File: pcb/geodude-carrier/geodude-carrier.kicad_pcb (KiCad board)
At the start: 2 copper layers, 112.5 x 135.2 mm, 43 parts, among them J1 12V, J2 12V, J3 GND, J31 SCL, J32 SDA, J34 3V3, J37 5V, J39 GND_L, J4 GND, J40 SCL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

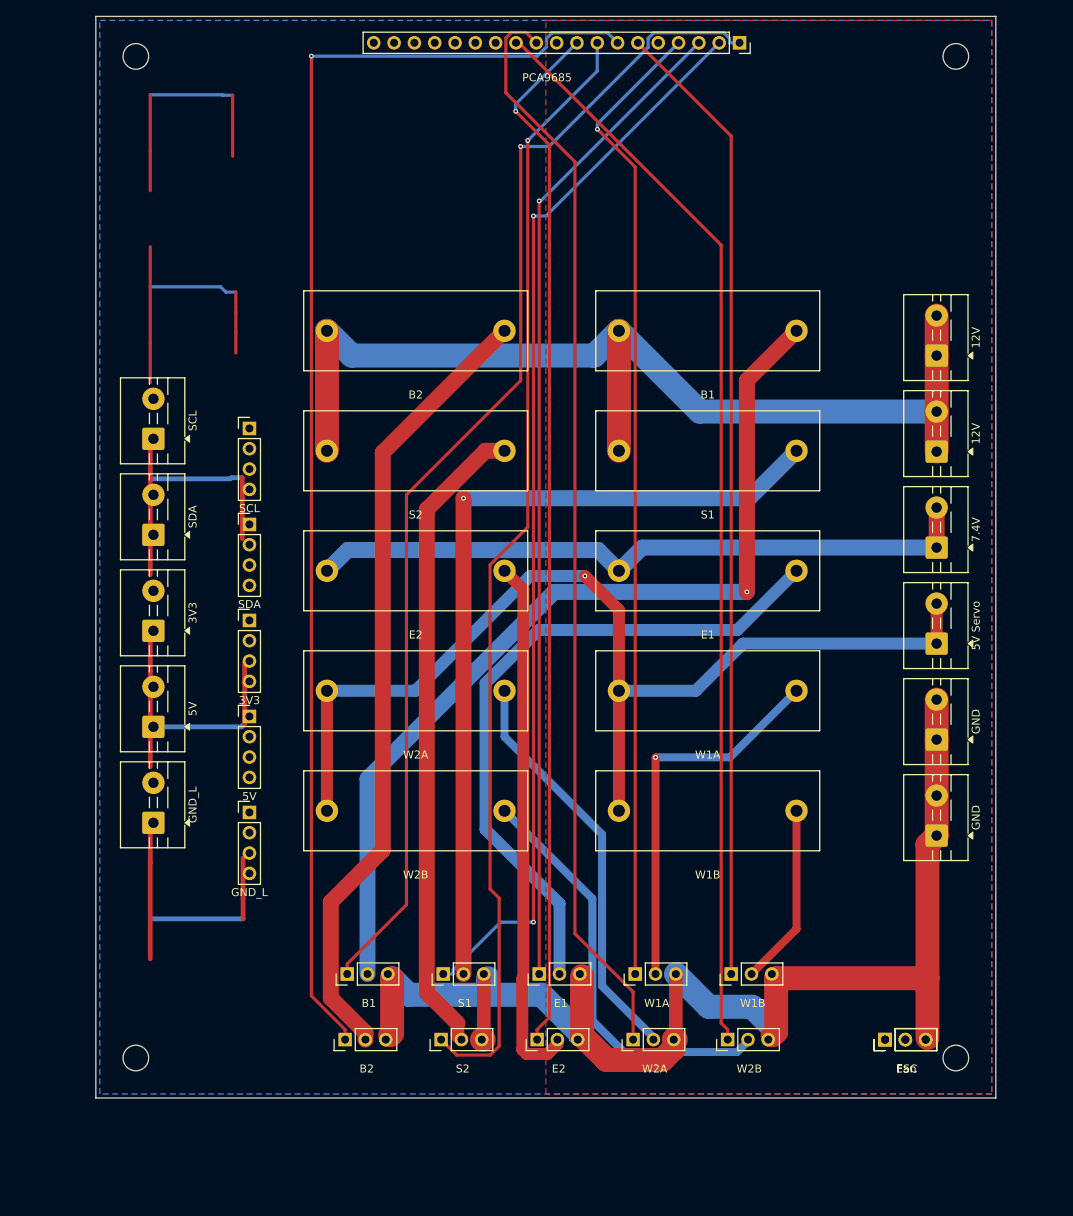
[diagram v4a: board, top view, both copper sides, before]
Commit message: Mounting holes 50mm horizontal spacing, centred
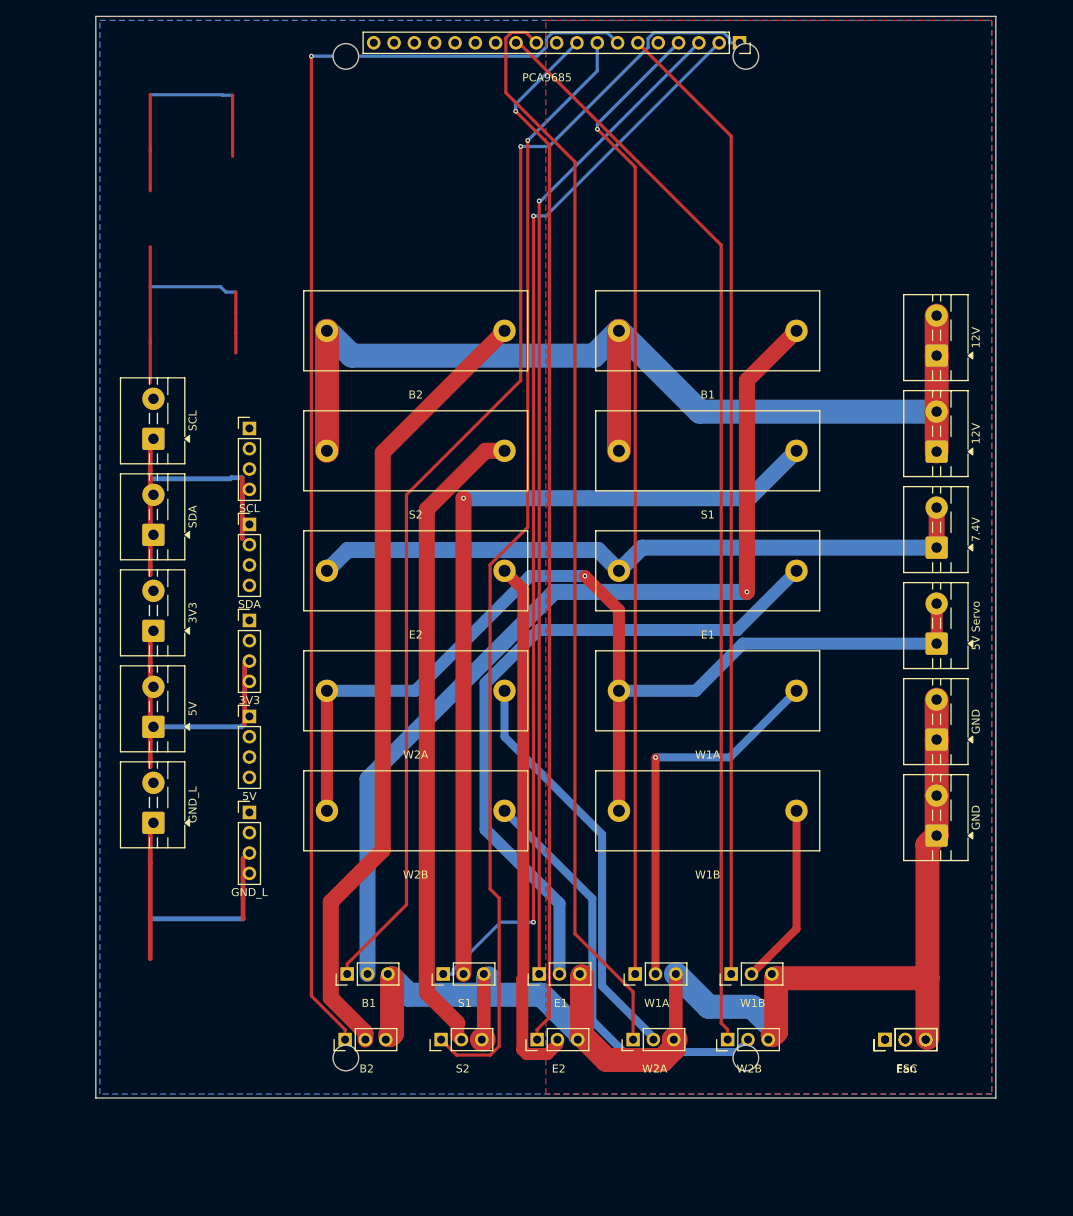
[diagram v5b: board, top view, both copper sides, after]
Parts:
- moved MH2 26.2 mm to (99.0, 9.60)
- moved MH4 26.2 mm to (99.0, 134.8)
- moved MH1 26.2 mm to (49.0, 9.60)
- moved MH3 26.2 mm to (49.0, 134.8)
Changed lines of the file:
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@@
 	(footprint "MountingHole_3.2mm_M3"
 		(layer "F.Cu")
-		(at 22.8 134.8)
+		(at 49.05 134.8)
 		(descr "Mounting Hole 3.2mm, M3, no annular, generated by kicad-footprint-generator mountinghole.py")
 		(tags "mountinghole M3")
@@
 	(footprint "MountingHole_3.2mm_M3"
 		(layer "F.Cu")
-		(at 22.8 9.6)
+		(at 49.05 9.6)
 		(descr "Mounting Hole 3.2mm, M3, no annular, generated by kicad-footprint-generator mountinghole.py")
 		(tags "mountinghole M3")
@@
 	(footprint "MountingHole_3.2mm_M3"
 		(layer "F.Cu")
-		(at 125.3 9.6)
+		(at 99.05 9.6)
 		(descr "Mounting Hole 3.2mm, M3, no annular, generated by kicad-footprint-generator mountinghole.py")
 		(tags "mountinghole M3")
@@
 	(footprint "MountingHole_3.2mm_M3"
 		(layer "F.Cu")
-		(at 125.3 134.8)
+		(at 99.05 134.8)
 		(descr "Mounting Hole 3.2mm, M3, no annular, generated by kicad-footprint-generator mountinghole.py")
 		(tags "mountinghole M3")

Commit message: Placement update
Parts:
- moved MH1 22.2 mm to (48.3, 31.8)
- moved MH2 22.0 mm to (99.8, 31.6)
- moved J_PCA 16.1 mm to (98.2, 24.0)
- moved MH3 5.71 mm to (49.3, 140.5)
- moved MH4 5.71 mm to (99.3, 140.5)
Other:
- board size 112.5 x 135.2 mm -> 112.5 x 140.8 mm
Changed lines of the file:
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@@
 	(footprint "MountingHole_3.2mm_M3"
 		(layer "F.Cu")
-		(at 49.05 134.8)
+		(at 49.3 140.5)
 		(descr "Mounting Hole 3.2mm, M3, no annular, generated by kicad-footprint-generator mountinghole.py")
 		(tags "mountinghole M3")
@@
 	(footprint "MountingHole_3.2mm_M3"
 		(layer "F.Cu")
-		(at 49.05 9.6)
+		(at 48.3 31.8)
 		(descr "Mounting Hole 3.2mm, M3, no annular, generated by kicad-footprint-generator mountinghole.py")
 		(tags "mountinghole M3")
@@
 	(footprint "MountingHole_3.2mm_M3"
 		(layer "F.Cu")
-		(at 99.05 9.6)
+		(at 99.8 31.6)
 		(descr "Mounting Hole 3.2mm, M3, no annular, generated by kicad-footprint-generator mountinghole.py")
 		(tags "mountinghole M3")
@@
 	(footprint "MountingHole_3.2mm_M3"
 		(layer "F.Cu")
-		(at 99.05 134.8)
+		(at 99.3 140.5)
 		(descr "Mounting Hole 3.2mm, M3, no annular, generated by kicad-footprint-generator mountinghole.py")
 		(tags "mountinghole M3")
@@
 	(footprint "PinSocket_1x19_P2.54mm_Vertical"
 		(layer "F.Cu")
-		(at 98.26 7.9 -90)
+		(at 98.16 24 -90)
 		(descr "Through hole straight socket strip, 1x19, 2.54mm pitch, single row (from Kicad 4.0.7), script generated")
 		(tags "Through hole socket strip THT 1x19 2.54mm single row")
@@
 	(gr_rect
 		(start 17.8 4.6)
-		(end 130.3 139.8)
+		(end 130.3 145.4)
 		(stroke
 			(width 0.1)

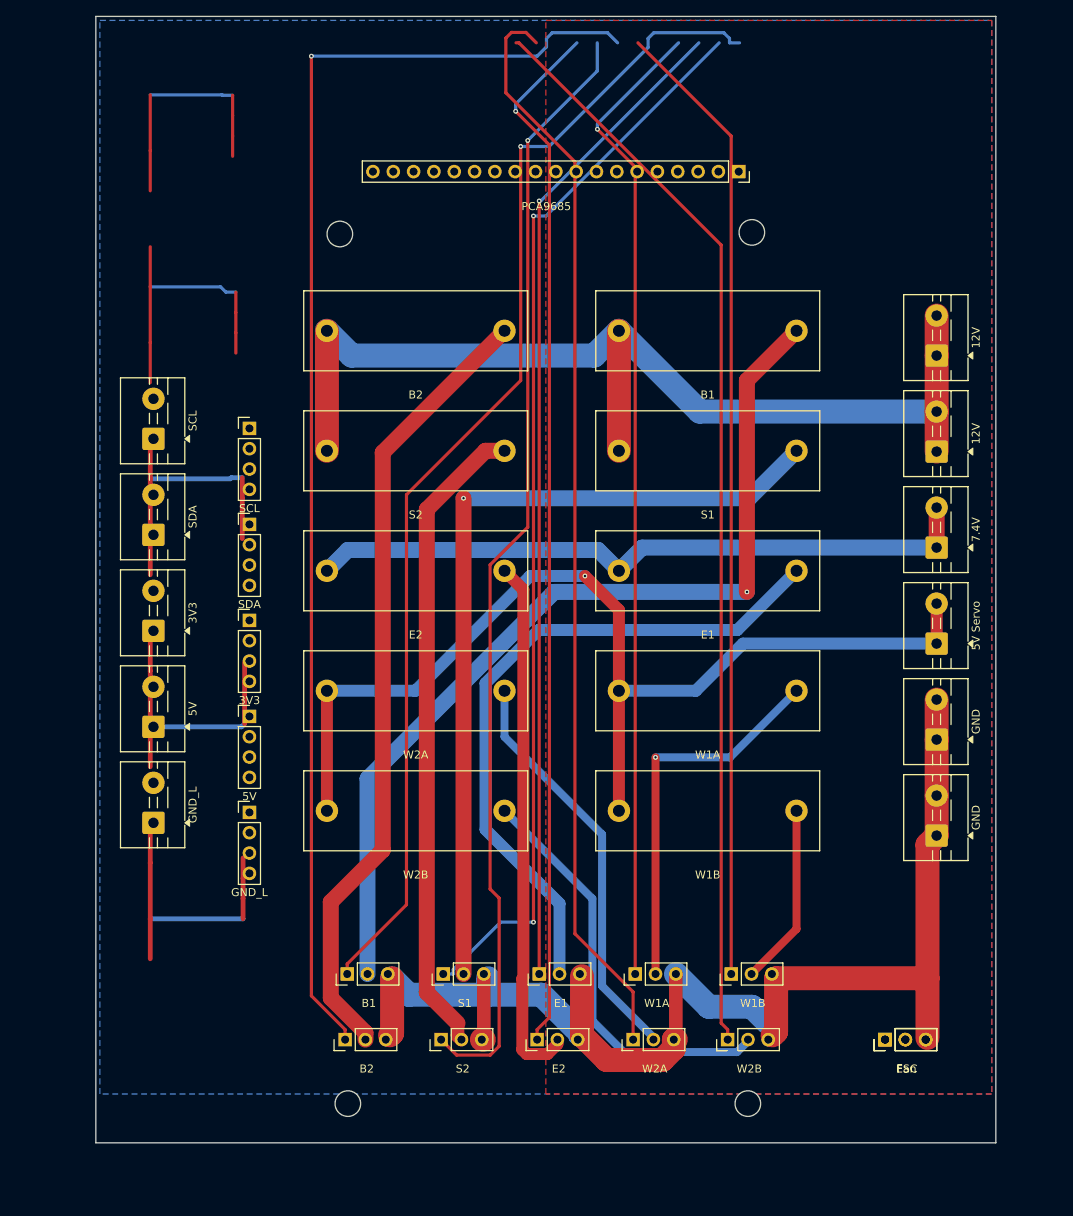
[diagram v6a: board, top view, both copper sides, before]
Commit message: Routed, bigger silk, ESC/Fan fixed, Gerbers - 5 unconnected need manual route
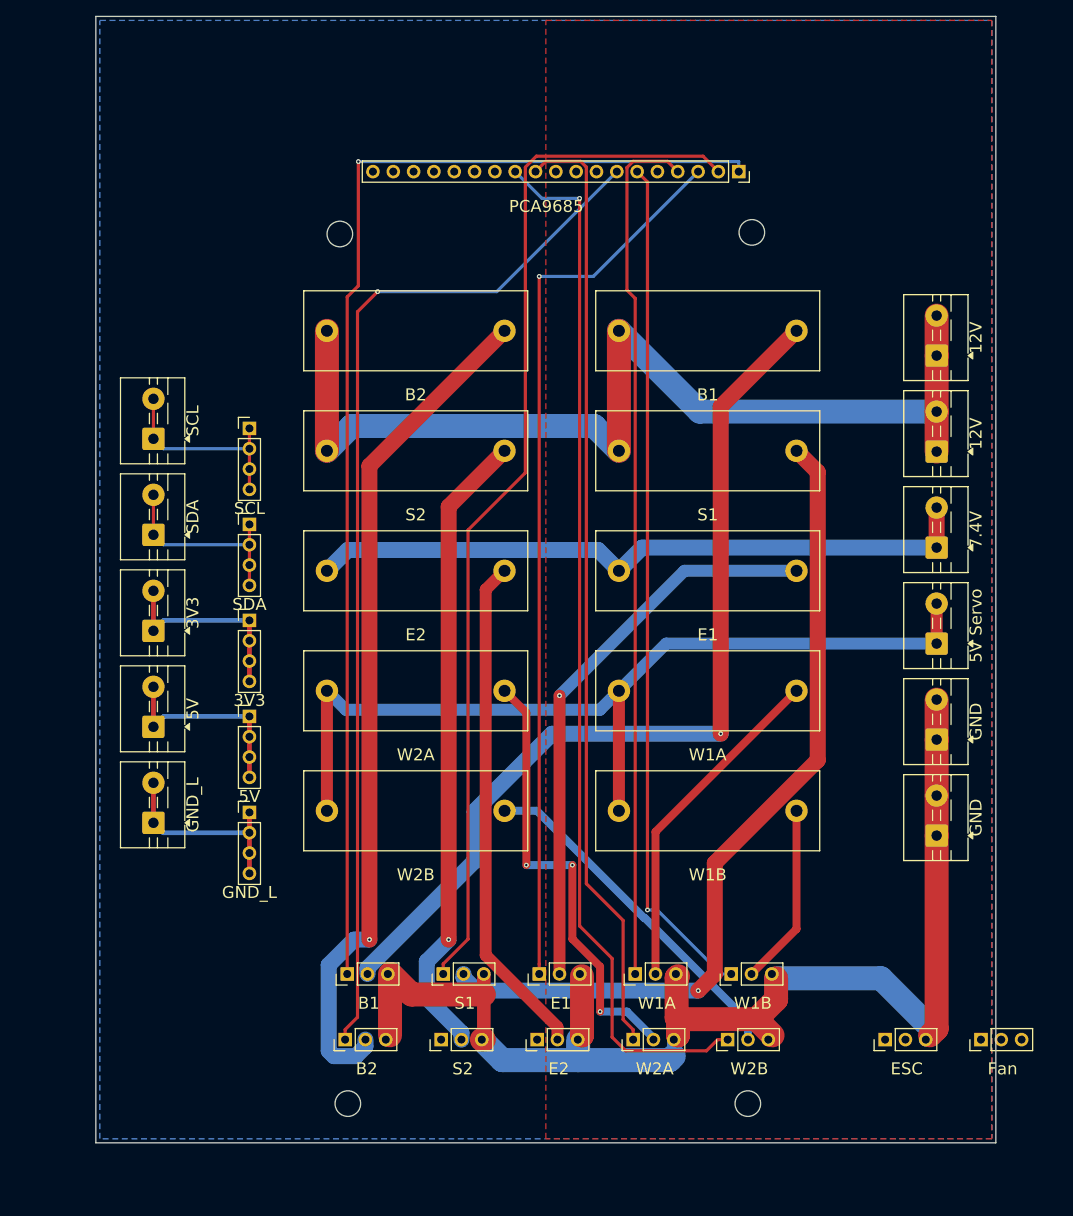
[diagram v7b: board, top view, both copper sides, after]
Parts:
- moved J_FAN 12.0 mm to (128.4, 132.5)
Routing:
- net PWM_CH6: track 140.0 -> 0.00 mm, vias 1 -> 0
- net PWM_CH7: track 130.2 -> 0.00 mm, vias 1 -> 0
- net PWM_CH5: track 165.3 -> 131.3 mm
- net GND_LOGIC: track 53.2 -> 25.1 mm
- net PWM_CH8: track 136.4 -> 118.7 mm
- net +5V_SERVO: track 131.5 -> 115.6 mm, vias 1 -> 0
- net PWM_CH4: track 121.2 -> 106.6 mm, vias 0 -> 1
- net PWM_CH3: track 122.6 -> 108.4 mm, vias 1 -> 0
- net SV3_PWR: track 84.9 -> 70.9 mm, vias 0 -> 1
- net PWM_CH2: track 124.8 -> 112.5 mm
- net +3V3: track 36.2 -> 25.2 mm
- net SDA: track 35.6 -> 25.1 mm
- net SV10_PWR: track 52.6 -> 43.6 mm
- net SV6_PWR: track 99.4 -> 106.5 mm, vias 0 -> 1
- net +5V_LOGIC: track 19.6 -> 25.2 mm
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
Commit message: Spread out layout, fan above ESC, 244 tracks, 1 unconnected PWM, Gerbers ready
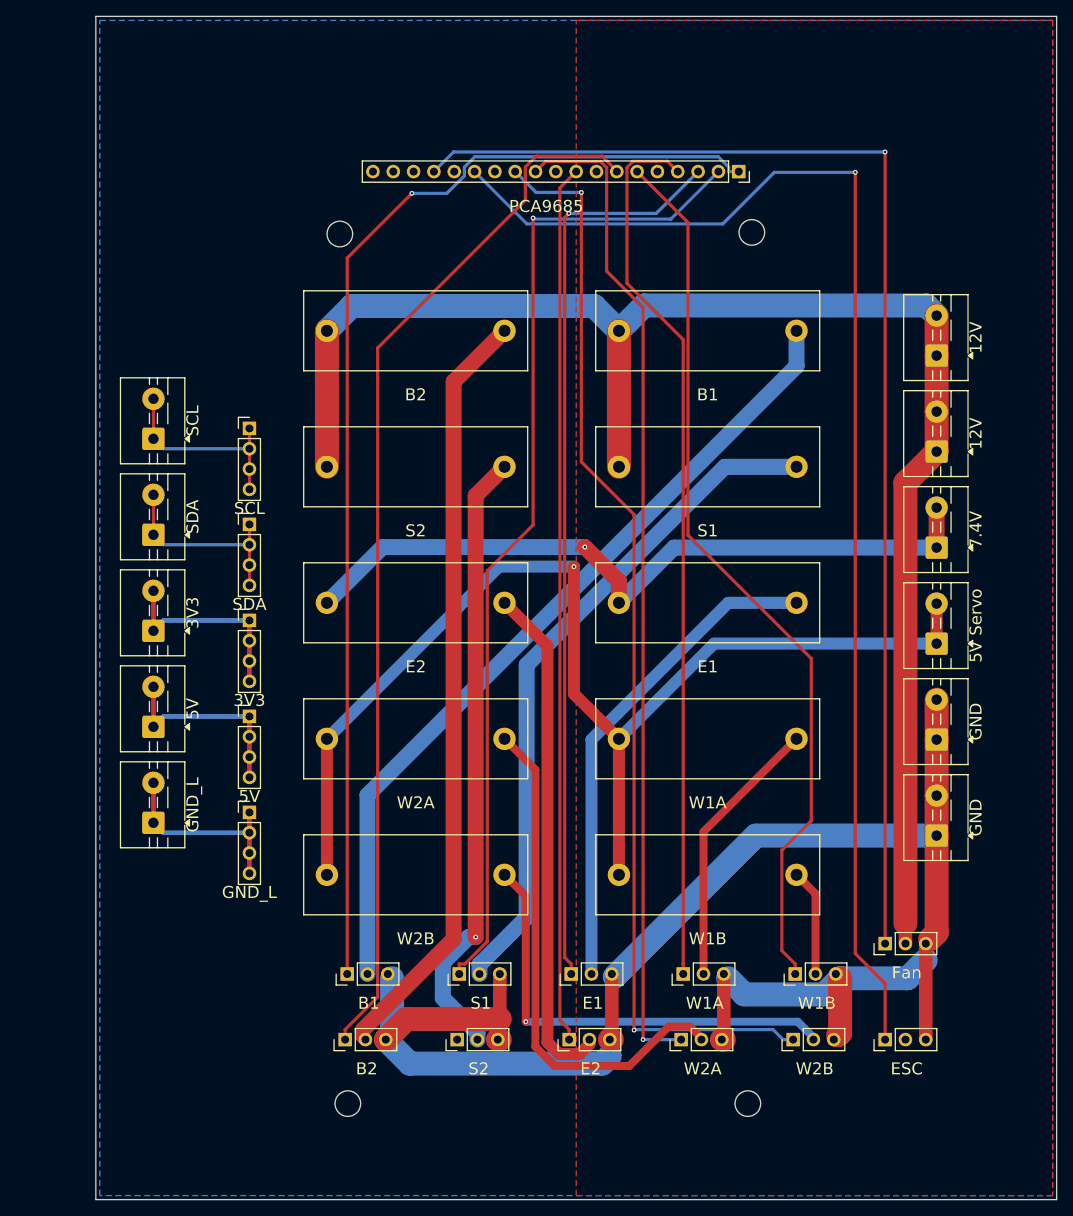
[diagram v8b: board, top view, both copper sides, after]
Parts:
- moved J_FAN 17.0 mm to (116.5, 120.5)
- moved SV10 8.18 mm to (105.0, 132.5)
- moved F10 8.00 mm to (57.8, 111.9)
- moved F5 8.00 mm to (94.3, 111.9)
- moved SV5 8.00 mm to (105.2, 124.3)
- moved F4 6.00 mm to (94.3, 94.9)
- moved F9 6.00 mm to (57.8, 94.9)
- moved SV4 6.00 mm to (91.2, 124.3)
- moved SV9 6.00 mm to (91.0, 132.5)
- moved F3 4.00 mm to (94.3, 77.9)
- moved F8 4.00 mm to (57.8, 77.9)
- moved SV3 4.00 mm to (77.2, 124.3)
- moved SV8 4.00 mm to (77.0, 132.5)
- moved F2 2.00 mm to (94.3, 60.9)
- moved F7 2.00 mm to (57.8, 60.9)
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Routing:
- net PWM_CH11: track 0.00 -> 162.9 mm, vias 0 -> 1
- net PWM_CH12: track 0.00 -> 156.4 mm, vias 0 -> 1
- net PWM_CH7: track 0.00 -> 109.8 mm
- net +12V: track 130.0 -> 194.7 mm
- net GND: track 164.4 -> 211.9 mm
- net +5V_SERVO: track 115.6 -> 147.3 mm, vias 0 -> 1
- net SV2_PWR: track 105.2 -> 85.1 mm, vias 1 -> 0
- net SV10_PWR: track 43.6 -> 56.5 mm, vias 0 -> 1
- net SV1_PWR: track 115.0 -> 102.6 mm, vias 1 -> 0
- net SV6_PWR: track 106.5 -> 96.1 mm, vias 1 -> 0
- net SV5_PWR: track 22.7 -> 13.4 mm
- net SV3_PWR: track 70.9 -> 62.0 mm, vias 1 -> 0
- net SV4_PWR: track 42.7 -> 34.2 mm
- net SV9_PWR: track 56.7 -> 64.7 mm, vias 3 -> 0
- net +7V4: track 84.6 -> 91.4 mm, vias 0 -> 1
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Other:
- board size 112.5 x 140.8 mm -> 120.1 x 147.9 mm
